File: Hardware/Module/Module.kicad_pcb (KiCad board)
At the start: 2 copper layers, 30 x 30 mm, 14 parts, among them J1 CONN_01X01, J2 CONN_02X03, J3 CONN_01X04, U1 74LS353

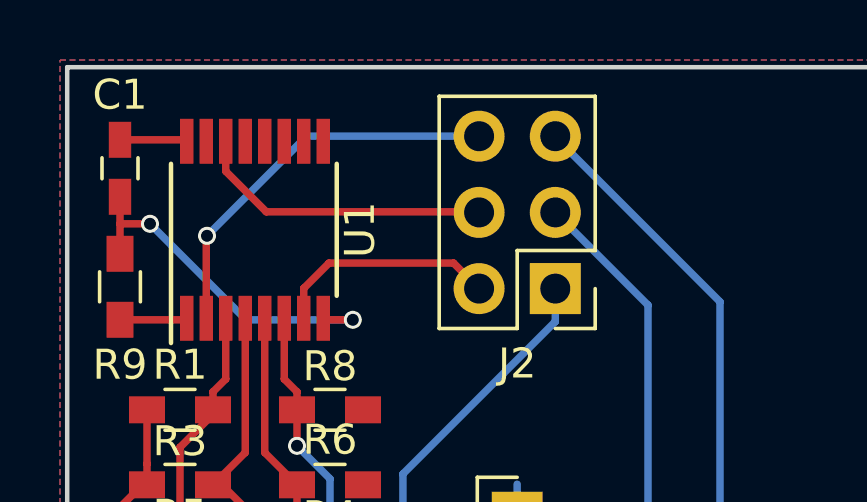
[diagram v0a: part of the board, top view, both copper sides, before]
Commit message: Hardware: Fix missing VCC connection
Signed-off-by: Paul Kocialkowski <contact@paulk.fr>
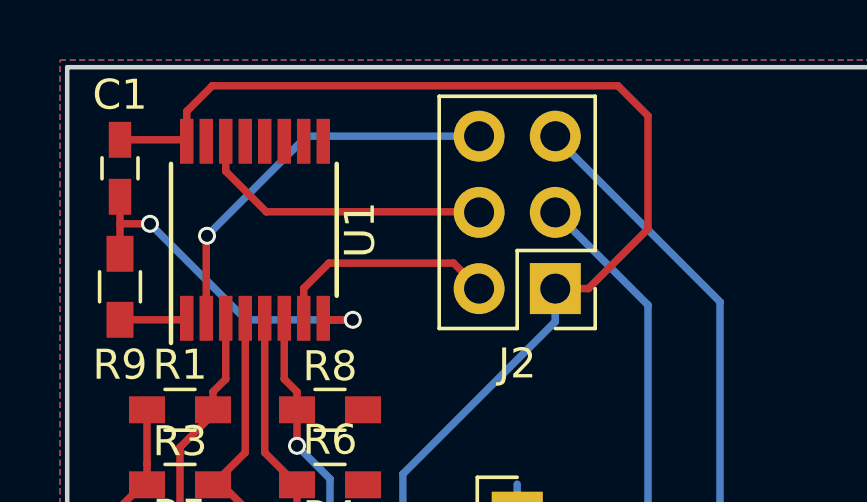
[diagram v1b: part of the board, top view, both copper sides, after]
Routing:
- net VCC: track 38.9 -> 63.8 mm
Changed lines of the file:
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@@
   (general
     (links 29)
-    (no_connects 8)
+    (no_connects 1)
     (area 126.525 52.575 157.480001 83.820001)
     (thickness 1.6)
     (drawings 6)
-    (tracks 89)
+    (tracks 96)
     (zones 0)
     (modules 14)
@@
   (segment (start 129 59.8) (end 129 58.8) (width 0.25) (layer F.Cu) (net 1))
   (segment (start 129 58.8) (end 129 57.9) (width 0.25) (layer F.Cu) (net 1))
+  (segment (start 145.6 54.2) (end 132.075 54.2) (width 0.25) (layer F.Cu) (net 2))
+  (segment (start 132.075 54.2) (end 131.225 55.05) (width 0.25) (layer F.Cu) (net 2))
+  (segment (start 131.225 55.05) (end 131.225 56.05) (width 0.25) (layer F.Cu) (net 2))
+  (segment (start 146.6 55.2) (end 145.6 54.2) (width 0.25) (layer F.Cu) (net 2))
+  (segment (start 146.6 58.97) (end 146.6 55.2) (width 0.25) (layer F.Cu) (net 2))
+  (segment (start 143.51 60.96) (end 144.61 60.96) (width 0.25) (layer F.Cu) (net 2))
+  (segment (start 144.61 60.96) (end 146.6 58.97) (width 0.25) (layer F.Cu) (net 2))
   (segment (start 138.43 76.2) (end 138.43 67.14) (width 0.25) (layer B.Cu) (net 2))
   (segment (start 138.43 67.14) (end 143.51 62.06) (width 0.25) (layer B.Cu) (net 2))
@@
     (connect_pads (clearance 0.508))
     (min_thickness 0.254)
-    (fill yes (arc_segments 16) (thermal_gap 0.508) (thermal_bridge_width 0.508))
+    (fill (arc_segments 16) (thermal_gap 0.508) (thermal_bridge_width 0.508))
     (polygon
       (pts
@@
     (connect_pads (clearance 0.508))
     (min_thickness 0.254)
-    (fill yes (arc_segments 16) (thermal_gap 0.508) (thermal_bridge_width 0.508))
+    (fill (arc_segments 16) (thermal_gap 0.508) (thermal_bridge_width 0.508))
     (polygon
       (pts
